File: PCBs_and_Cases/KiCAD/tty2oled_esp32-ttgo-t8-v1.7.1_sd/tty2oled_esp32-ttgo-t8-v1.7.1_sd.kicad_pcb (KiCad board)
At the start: 2 copper layers, 35.6 x 99.7 mm, 2 parts

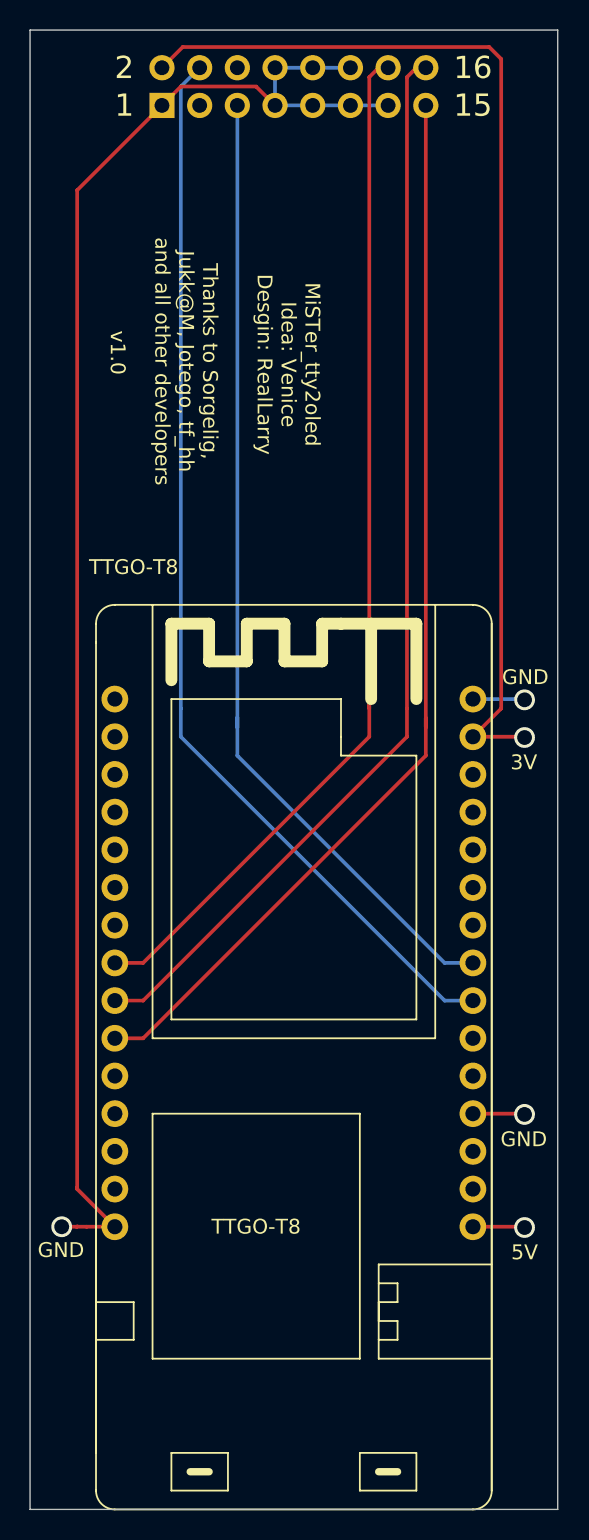
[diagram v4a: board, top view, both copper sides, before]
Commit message: Update board esp32-TTGo to v1.1
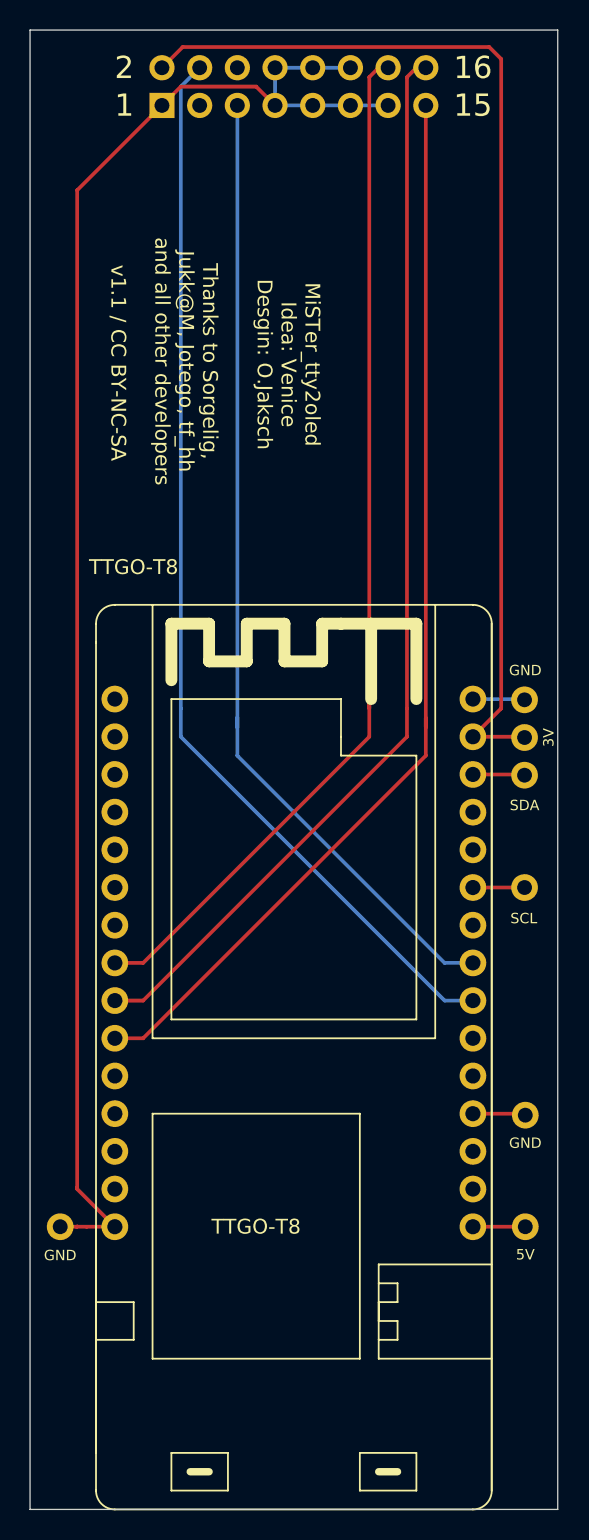
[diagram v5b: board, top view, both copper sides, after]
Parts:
- added REF**: SolderWirePad_single_0-8mmDrill, Wire_Pads:SolderWirePad_single_0-8mmDrill, F.Cu at (165.4, 101.7)
- added REF**: SolderWirePad_single_0-8mmDrill, Wire_Pads:SolderWirePad_single_0-8mmDrill, F.Cu at (165.4, 109.2)
- added REF**: SolderWirePad_single_0-8mmDrill, Wire_Pads:SolderWirePad_single_0-8mmDrill, F.Cu at (165.4, 96.6)
- added REF**: SolderWirePad_single_0-8mmDrill, Wire_Pads:SolderWirePad_single_0-8mmDrill, F.Cu at (165.4, 99.1)
- added REF**: SolderWirePad_single_0-8mmDrill, Wire_Pads:SolderWirePad_single_0-8mmDrill, F.Cu at (165.5, 124.6)
- added REF**: SolderWirePad_single_0-8mmDrill, Wire_Pads:SolderWirePad_single_0-8mmDrill, F.Cu at (165.5, 132.1)
- added REF**: SolderWirePad_single_0-8mmDrill, Wire_Pads:SolderWirePad_single_0-8mmDrill, F.Cu at (134.1, 132.1)
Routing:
- net (no net): track 543.8 -> 550.5 mm, vias 5 -> 0
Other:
- board text added: "MiSTer_tty2oled Idea: Venice Desgin: O.Jaksch"
- board text added: "SCL"
- board text added: "SDA"
- board text added: "v1.1 / CC BY-NC-SA"
- board text removed: "MiSTer_tty2oled Idea: Venice Desgin: RealLarry"
- board text removed: "v1.0"
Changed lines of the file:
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@@
   (general
     (thickness 1.6)
-    (drawings 19)
-    (tracks 57)
+    (drawings 21)
+    (tracks 51)
     (zones 0)
-    (modules 2)
+    (modules 9)
     (nets 1)
   )
@@
     (mod_text_size 1 1)
     (mod_text_width 0.15)
-    (pad_size 1.7 1.7)
+    (pad_size 1.8 1.8)
     (pad_drill 1)
     (pad_to_mask_clearance 0)
@@
     (uvia_dia 0.3)
     (uvia_drill 0.1)
+  )
+  (module Wire_Pads:SolderWirePad_single_0-8mmDrill (layer F.Cu)
+    (at 165.4048 101.6508)
+    (fp_text reference REF** (at 0 -2.54) (layer F.SilkS) hide
+      (effects (font (size 1 1) (thickness 0.15)))
+    )
+    (fp_text value SolderWirePad_single_0-8mmDrill (at 0 2.54) (layer F.Fab) hide
+      (effects (font (size 1 1) (thickness 0.15)))
+    )
+    (pad 1 thru_hole circle (at 0 0) (size 1.8 1.8) (drill 1) (layers *.Cu *.Mask))
+  )
+  (module Wire_Pads:SolderWirePad_single_0-8mmDrill (layer F.Cu)
+    (at 165.4048 109.22)
+    (fp_text reference REF** (at 0 -2.54) (layer F.SilkS) hide
+      (effects (font (size 1 1) (thickness 0.15)))
+    )
+    (fp_text value SolderWirePad_single_0-8mmDrill (at 0 2.54) (layer F.Fab) hide
+      (effects (font (size 1 1) (thickness 0.15)))
+    )
+    (pad 1 thru_hole circle (at 0 0) (size 1.8 1.8) (drill 1) (layers *.Cu *.Mask))
+  )
+  (module Wire_Pads:SolderWirePad_single_0-8mmDrill (layer F.Cu)
+    (at 165.4048 96.5708)
+    (fp_text reference REF** (at 0 -2.54) (layer F.SilkS) hide
+      (effects (font (size 1 1) (thickness 0.15)))
+    )
+    (fp_text value SolderWirePad_single_0-8mmDrill (at 0 2.54) (layer F.Fab) hide
+      (effects (font (size 1 1) (thickness 0.15)))
+    )
+    (pad 1 thru_hole circle (at 0 0) (size 1.8 1.8) (drill 1) (layers *.Cu *.Mask))
+  )
+  (module Wire_Pads:SolderWirePad_single_0-8mmDrill (layer F.Cu)
+    (at 165.4048 99.1108)
+    (fp_text reference REF** (at 0 -2.54) (layer F.SilkS) hide
+      (effects (font (size 1 1) (thickness 0.15)))
+    )
+    (fp_text value SolderWirePad_single_0-8mmDrill (at 0 2.54) (layer F.Fab) hide
+      (effects (font (size 1 1) (thickness 0.15)))
+    )
+    (pad 1 thru_hole circle (at 0 0) (size 1.8 1.8) (drill 1) (layers *.Cu *.Mask))
+  )
+  (module Wire_Pads:SolderWirePad_single_0-8mmDrill (layer F.Cu)
+    (at 165.4556 124.5616)
+    (fp_text reference REF** (at 0 -2.54) (layer F.SilkS) hide
+      (effects (font (size 1 1) (thickness 0.15)))
+    )
+    (fp_text value SolderWirePad_single_0-8mmDrill (at 0 2.54) (layer F.Fab) hide
+      (effects (font (size 1 1) (thickness 0.15)))
+    )
+    (pad 1 thru_hole circle (at 0 0) (size 1.8 1.8) (drill 1) (layers *.Cu *.Mask))
+  )
+  (module Wire_Pads:SolderWirePad_single_0-8mmDrill (layer F.Cu)
+    (at 165.4556 132.08)
+    (fp_text reference REF** (at 0 -2.54) (layer F.SilkS) hide
+      (effects (font (size 1 1) (thickness 0.15)))
+    )
+    (fp_text value SolderWirePad_single_0-8mmDrill (at 0 2.54) (layer F.Fab) hide
+      (effects (font (size 1 1) (thickness 0.15)))
+    )
+    (pad 1 thru_hole circle (at 0 0) (size 1.8 1.8) (drill 1) (layers *.Cu *.Mask))
+  )
+  (module Wire_Pads:SolderWirePad_single_0-8mmDrill (layer F.Cu)
+    (at 134.112 132.08)
+    (fp_text reference REF** (at 0 -2.54) (layer F.SilkS) hide
+      (effects (font (size 1 1) (thickness 0.15)))
+    )
+    (fp_text value SolderWirePad_single_0-8mmDrill (at 0 2.54) (layer F.Fab) hide
+      (effects (font (size 1 1) (thickness 0.15)))
+    )
+    (pad 1 thru_hole circle (at 0 0) (size 1.8 1.8) (drill 1) (layers *.Cu *.Mask))
   )
   (module ttgo:TTGO-T8 (layer F.Cu)
@@
     )
   )
-  (gr_text GND (at 134.1628 133.6548) (layer F.SilkS)
+  (gr_text SDA (at 165.4048 103.6828) (layer F.SilkS)
+    (effects (font (size 0.7 0.7) (thickness 0.15)))
+  )
+  (gr_text SCL (at 165.354 111.3028) (layer F.SilkS)
+    (effects (font (size 0.7 0.7) (thickness 0.15)))
+  )
+  (target plus (at 132.08 151.13) (size 5) (width 0.05) (layer Edge.Cuts))
+  (gr_text GND (at 134.112 134.0104) (layer F.SilkS)
+    (effects (font (size 0.7 0.7) (thickness 0.15)))
+  )
+  (gr_text 5V (at 165.4556 133.9596) (layer F.SilkS)
+    (effects (font (size 0.7 0.7) (thickness 0.15)))
+  )
+  (gr_text GND (at 165.4556 126.4412) (layer F.SilkS)
+    (effects (font (size 0.7 0.7) (thickness 0.15)))
+  )
+  (gr_text 3V (at 167.0304 99.1108 90) (layer F.SilkS)
+    (effects (font (size 0.7 0.7) (thickness 0.15)))
+  )
+  (gr_text GND (at 165.4556 94.5896) (layer F.SilkS)
+    (effects (font (size 0.7 0.7) (thickness 0.15)))
+  )
+  (gr_text "v1.1 / CC BY-NC-SA" (at 138.0236 73.8632 -90) (layer F.SilkS)
     (effects (font (size 1 1) (thickness 0.15)))
   )
-  (gr_text 5V (at 165.4048 133.8072) (layer F.SilkS)
-    (effects (font (size 1 1) (thickness 0.15)))
-  )
-  (gr_text GND (at 165.354 126.1872) (layer F.SilkS)
-    (effects (font (size 1 1) (thickness 0.15)))
-  )
-  (gr_text 3V (at 165.354 100.7872) (layer F.SilkS)
-    (effects (font (size 1 1) (thickness 0.15)))
-  )
-  (gr_text GND (at 165.4556 95.0468) (layer F.SilkS)
-    (effects (font (size 1 1) (thickness 0.15)))
-  )
-  (gr_text v1.0 (at 137.9855 73.1774 -90) (layer F.SilkS)
-    (effects (font (size 1 1) (thickness 0.15)))
-  )
-  (gr_text "MiSTer_tty2oled\nIdea: Venice\nDesgin: RealLarry" (at 149.4917 73.9648 -90) (layer F.SilkS)
+  (gr_text "MiSTer_tty2oled\nIdea: Venice\nDesgin: O.Jaksch" (at 149.4917 73.9648 -90) (layer F.SilkS)
     (effects (font (size 1 1) (thickness 0.15)))
   )
@@
   (gr_line (start 167.64 51.435) (end 132.08 51.435) (layer Edge.Cuts) (width 0.05))
   (gr_line (start 132.08 151.13) (end 167.64 151.13) (layer Edge.Cuts) (width 0.05))
-  (target plus (at 132.08 151.13) (size 5) (width 0.05) (layer Edge.Cuts))
   (gr_text 16 (at 161.925 53.975) (layer F.SilkS)
     (effects (font (size 1.5 1.5) (thickness 0.3)))
@@
   (segment (start 148.59 56.515) (end 147.32 55.245) (width 0.25) (layer F.Cu) (net 0))
   (segment (start 147.32 55.245) (end 142.24 55.245) (width 0.25) (layer F.Cu) (net 0))
-  (via (at 134.2136 132.08) (size 1.4) (drill 1) (layers F.Cu B.Cu) (net 0))
   (segment (start 135.255 132.0546) (end 135.2296 132.08) (width 0.25) (layer F.Cu) (net 0))
   (segment (start 140.97 56.515) (end 135.255 62.23) (width 0.25) (layer F.Cu) (net 0))
   (segment (start 135.2296 132.08) (end 135.89 132.08) (width 0.25) (layer F.Cu) (net 0))
   (segment (start 134.2136 132.08) (end 135.2296 132.08) (width 0.25) (layer F.Cu) (net 0))
-  (via (at 165.4048 132.1308) (size 1.4) (drill 1) (layers F.Cu B.Cu) (net 0))
-  (via (at 165.4048 124.5108) (size 1.4) (drill 1) (layers F.Cu B.Cu) (net 0))
-  (via (at 165.4048 99.1108) (size 1.4) (drill 1) (layers F.Cu B.Cu) (net 0))
-  (via (at 165.4048 96.5708) (size 1.4) (drill 1) (layers F.Cu B.Cu) (net 0))
-  (segment (start 165.354 132.08) (end 165.4048 132.1308) (width 0.25) (layer F.Cu) (net 0))
   (segment (start 161.925 132.08) (end 165.354 132.08) (width 0.25) (layer F.Cu) (net 0))
-  (segment (start 165.354 124.46) (end 165.4048 124.5108) (width 0.25) (layer F.Cu) (net 0))
   (segment (start 161.925 124.46) (end 165.354 124.46) (width 0.25) (layer F.Cu) (net 0))
-  (segment (start 165.354 99.06) (end 165.4048 99.1108) (width 0.25) (layer F.Cu) (net 0))
   (segment (start 161.925 99.06) (end 165.354 99.06) (width 0.25) (layer F.Cu) (net 0))
-  (segment (start 165.354 96.52) (end 165.4048 96.5708) (width 0.25) (layer B.Cu) (net 0))
   (segment (start 161.925 96.52) (end 165.354 96.52) (width 0.25) (layer B.Cu) (net 0))
   (segment (start 135.255 129.54) (end 135.255 129.413) (width 0.25) (layer F.Cu) (net 0))
   (segment (start 137.795 132.08) (end 135.255 129.54) (width 0.25) (layer F.Cu) (net 0))
   (segment (start 135.255 62.23) (end 135.255 129.413) (width 0.25) (layer F.Cu) (net 0))
+  (segment (start 161.925 109.22) (end 165.4048 109.22) (width 0.25) (layer F.Cu) (net 0))
+  (segment (start 165.354 101.6) (end 165.4048 101.6508) (width 0.25) (layer F.Cu) (net 0))
+  (segment (start 161.925 101.6) (end 165.354 101.6) (width 0.25) (layer F.Cu) (net 0))
 )

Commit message: PCB TTG0 shrunk by 0.8mm
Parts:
- TTGO-T8: value TTGO-T8 -> TTGO-T8 v1.7.1
